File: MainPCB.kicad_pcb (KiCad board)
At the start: 4 copper layers, 108 x 70 mm, 70 parts, among them IC1 VNH7070ASTR, IC2 VNH7070ASTR, IC3 VNH7070ASTR, IC4 VNH7070ASTR, J1 Conn_01x06, J10 Conn_01x02, J11 Conn_01x03, J12 Conn_01x04, J2 RaspberryPi, J3 Conn_01x02, J4 Conn_01x02, J5 Screw_Terminal_01x02, J6 Conn_02x05_Odd_Even, J7 Conn_01x03, J8 Conn_01x02, J9 Conn_01x02, M1 Motor_DC, M2 Motor_DC, M3 Motor_DC, M4 Motor_DC, SW1 SW_DPST_x2, SW2 SW_SPDT, SW3 SW_SPDT, SW4 SW_SPDT, SW5 SW_SPDT, U1 V_Regulator3.3v, U10 N channel, U12 Teensy4.1, U2 V_Regulator5v, U4 V_Regulator5v, U5 Compass

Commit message: Finished Main PCB
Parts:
- R12, R13, R14, R15, R16, R17: moved to F.Cu
- moved R14 5.65 mm to (93.0, 88.2), turned to -90 degrees
- moved J4 3.43 mm to (123.2, 124.1), turned to 90 degrees
- moved R13 2.63 mm to (91.0, 84.4), turned to -90 degrees
- moved J8 1.19 mm to (88.4, 66.6)
- moved U1 1.04 mm to (85.8, 79.5)
- moved C7 0.60 mm to (97.6, 72.3)
- moved R12 0.57 mm to (93.0, 84.4), turned to -90 degrees
- moved C8 0.34 mm to (97.6, 69.8)
- turned R15 to 0 degrees
- turned R16 to 0 degrees
- turned R17 to 0 degrees
- turned R11 to 0 degrees
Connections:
- IC1 pad 12: 12v -> 12V
- IC1 pad 4: 12v -> 12V
- IC1 pad 5: 12v -> 12V
- IC2 pad 12: 12v -> 12V
- IC2 pad 4: 12v -> 12V
- IC2 pad 5: 12v -> 12V
- IC3 pad 12: 12v -> 12V
- IC3 pad 4: 12v -> 12V
- IC3 pad 5: 12v -> 12V
- IC4 pad 12: 12v -> 12V
- IC4 pad 4: 12v -> 12V
- IC4 pad 5: 12v -> 12V
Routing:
- net GND: track 8.32 -> 492.6 mm, vias 0 -> 2
- net 5V: track 0.00 -> 278.0 mm
- net 3.3V: track 0.00 -> 268.0 mm, vias 0 -> 1
- net 12V: track 140.3 -> 388.4 mm, vias 0 -> 36
- net Net-(SW1A-B): track 4.74 -> 120.5 mm, vias 0 -> 1
- net SLIDE3: track 0.00 -> 82.9 mm
- net SLIDE1: track 0.00 -> 78.2 mm
- net TX2->RX: track 0.00 -> 77.9 mm
- net RX2->TX: track 0.00 -> 76.6 mm, vias 0 -> 1
- net ESC_PWM: track 0.00 -> 75.2 mm
- net SLIDE2: track 0.00 -> 67.9 mm
- net CS3: track 0.00 -> 67.6 mm, vias 0 -> 1
- net CS2: track 0.00 -> 63.9 mm
- net STATE: track 0.00 -> 61.7 mm, vias 0 -> 1
- net CS1: track 0.00 -> 61.3 mm, vias 0 -> 1
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- added copper zone on B.Cu, net GND
- added copper zone on F.Cu, net GND
- added copper zone on In1.Cu, net GND
- added copper zone on In2.Cu, net GND

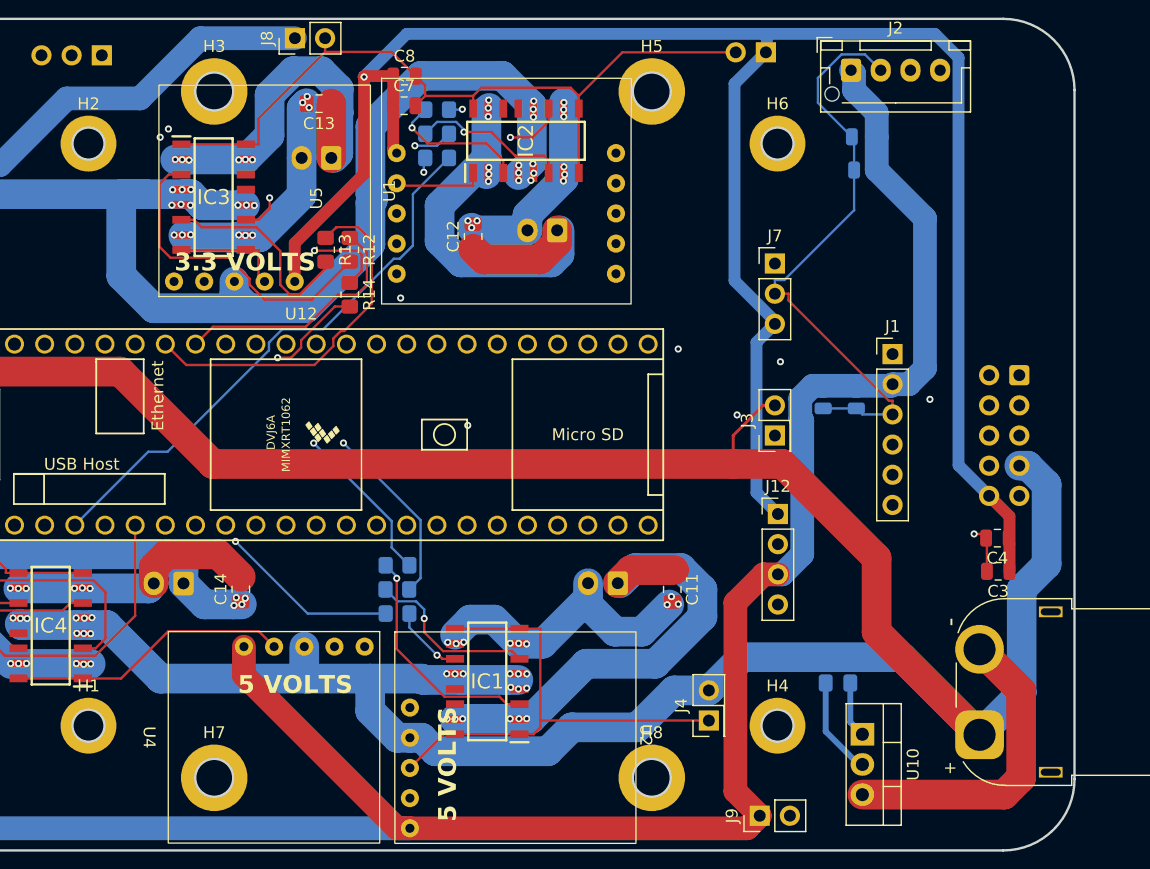
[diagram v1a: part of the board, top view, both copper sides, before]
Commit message: Fixed Holes error
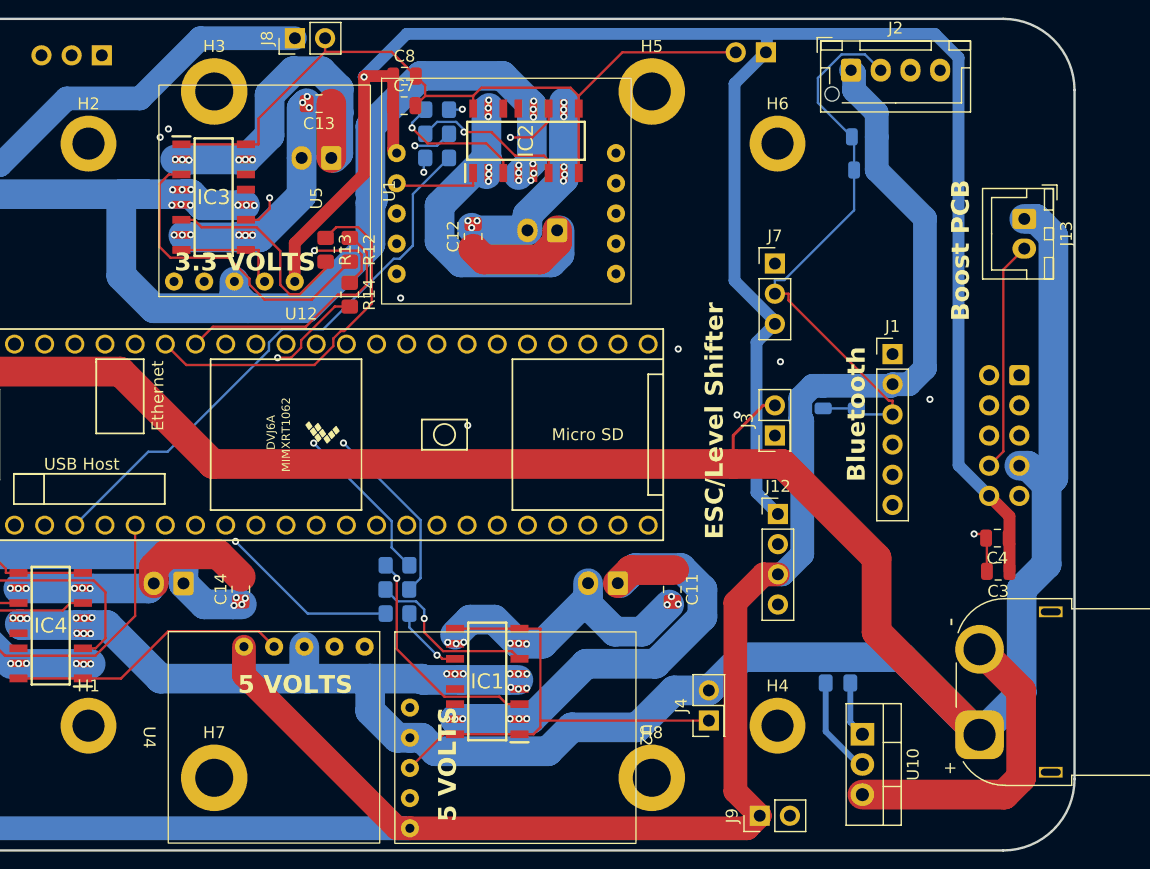
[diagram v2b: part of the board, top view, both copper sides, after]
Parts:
- added J13: Conn_01x02, Connector_JST:JST_XH_B2B-XH-A_1x02_P2.50mm_Vertical, F.Cu at (149.8, 81.8)
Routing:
- net 12V: track 388.4 -> 412.6 mm
- net GND: track 492.6 -> 512.1 mm
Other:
- outline, holes or cut-outs redrawn
- board text added: "Bluetooth"
- board text added: "Boost PCB"
- board text added: "ESC/Level Shifter"

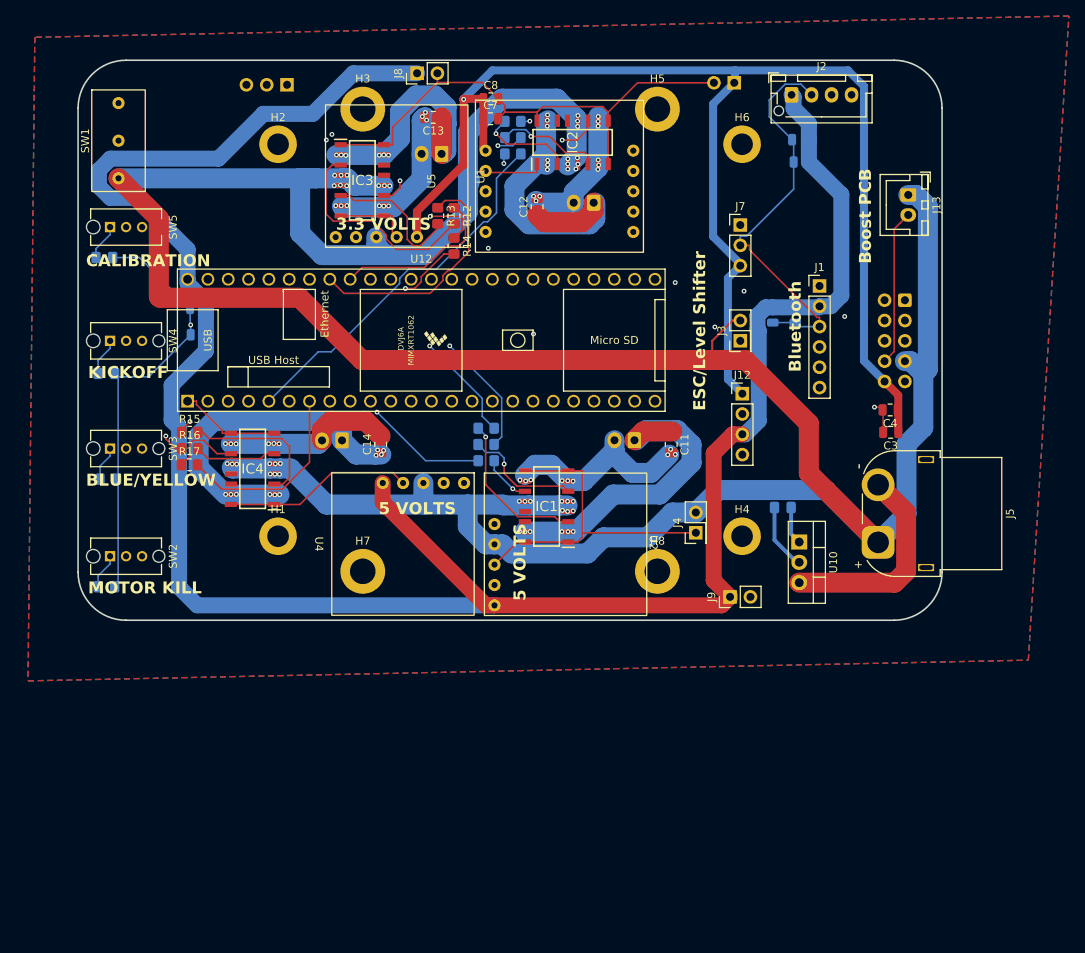
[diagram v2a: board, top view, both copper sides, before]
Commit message: Added Boost Converter
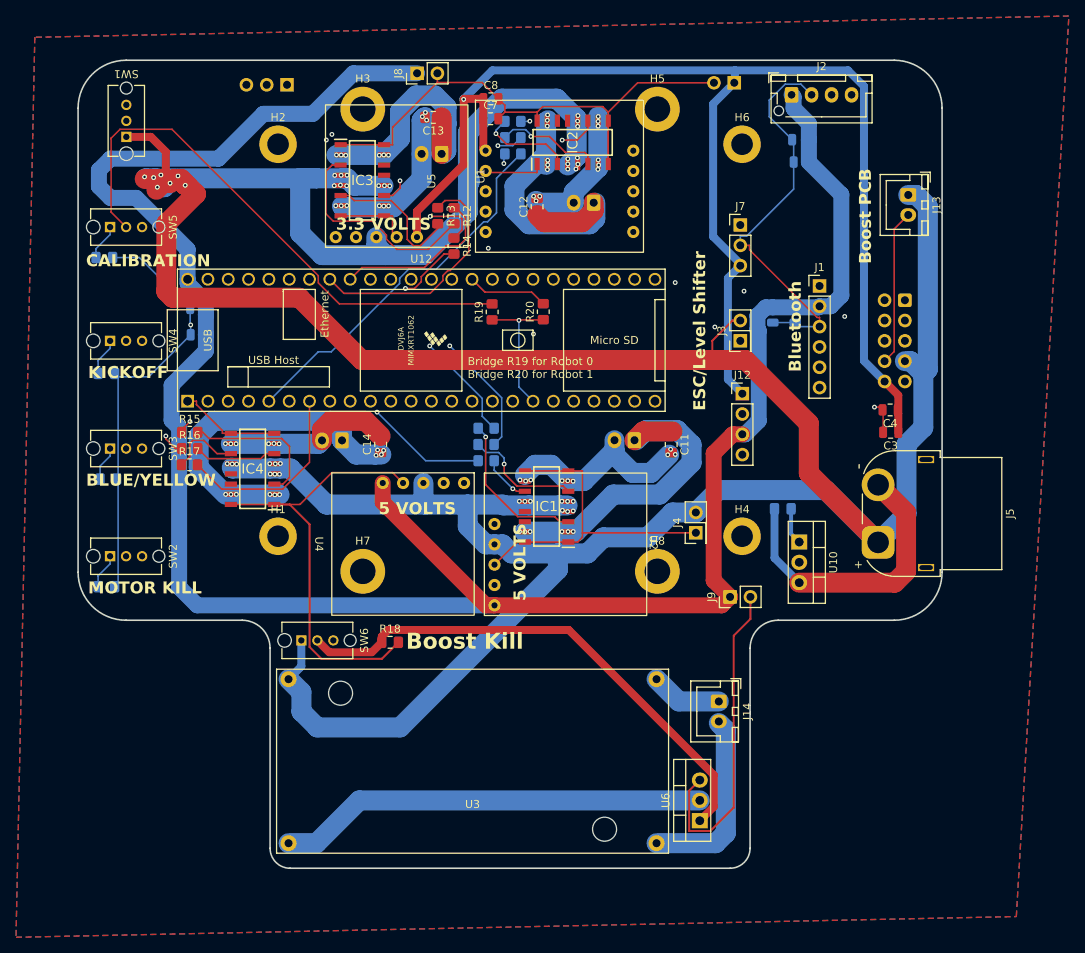
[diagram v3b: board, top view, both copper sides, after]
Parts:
- added J14: Conn_01x02, Connector_JST:JST_XH_B2B-XH-A_1x02_P2.50mm_Vertical, F.Cu at (126.1, 145.2)
- added R18: 10k, Capacitor_SMD:C_0805_2012Metric_Pad1.18x1.45mm_HandSolder, F.Cu at (85.0, 137.8)
- added R19: 0, Resistor_SMD:R_0805_2012Metric_Pad1.20x1.40mm_HandSolder, F.Cu at (97.8, 96.5)
- added R20: 1, Resistor_SMD:R_0805_2012Metric_Pad1.20x1.40mm_HandSolder, F.Cu at (104.2, 96.4)
- added SW6: SW_DPST_x2, SlideSW:SPDT_OS102011_CNK, F.Cu at (73.9, 137.5)
- added U3: BoostConverter, BoostConverter:Boost_Convertor_LM2577, F.Cu at (95.3, 152.6)
- added U6: N channel, Package_TO_SOT_THT:TO-220-3_Vertical, F.Cu at (123.7, 160.1)
- SW1: footprint ToggleSwitch:ANT11SECQE -> SlideSW:SPDT_OS102011_CNK
- moved SW1 1.09 mm to (52.0, 74.6), turned to 180 degrees
- moved R2 0.17 mm to (134.1, 121.1)
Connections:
- R2 pad 2: GND -> Net-(J5-Pin_2)
- U12 pad 18: unconnected-(U12-26_A12_MOSI1-Pad18) -> SelectionPin
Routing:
- net GND: track 512.1 -> 588.4 mm
- net 3.3V: track 268.0 -> 344.2 mm
- net 12V: track 412.6 -> 478.6 mm, vias 36 -> 43
- net Net-(SW6A-B): track 0.00 -> 65.7 mm
- net Net-(U3-In-): track 0.00 -> 53.6 mm
- net Net-(J14-Pin_2): track 0.00 -> 23.3 mm
- net SelectionPin: track 0.00 -> 17.3 mm, vias 0 -> 1
- net Net-(J5-Pin_2): track 26.2 -> 36.7 mm
- net Net-(J14-Pin_1): track 0.00 -> 8.93 mm
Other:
- board size 108 x 70 mm -> 108 x 101 mm
- board text added: "Boost Kill"
- board text added: "Bridge R19 for Robot 0 Bridge R20 for Robot 1"

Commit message: Flipped JST Motor Connectors
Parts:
- M1, M2, M3, M4: moved to F.Cu
- moved M1 1.74 mm to (115.8, 114.2)
- moved M4 0.75 mm to (79.0, 113.3)
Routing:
- net 12V: track 478.6 -> 472.2 mm
- net Net-(IC1-OUT_A_1): track 46.6 -> 49.1 mm
- net Net-(IC1-OUT_B_1): track 28.4 -> 30.0 mm
- net Net-(IC4-OUT_B_1): track 22.2 -> 23.0 mm

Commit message: changed a lot
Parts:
- removed J12: Conn_01x04, Connector_PinHeader_2.54mm:PinHeader_1x04_P2.54mm_Vertical
- removed J3: Conn_01x02, Connector_PinHeader_2.54mm:PinHeader_2x01_P2.54mm_Vertical
- removed J7: Conn_01x03, Connector_PinHeader_2.54mm:PinHeader_1x03_P2.54mm_Vertical
- removed U5: Compass, Custom:Compass Sensor DFRobot
- added C15: 0.1uf, Capacitor_SMD:C_0805_2012Metric_Pad1.18x1.45mm_HandSolder, B.Cu at (139.7, 80.3)
- added IC5: VNH7070ASTR, VNH:SOIC127P600X175-16N, F.Cu at (130.8, 83.8)
- added J15: Conn_01x05, Connector_JST:JST_XH_B5B-XH-A_1x05_P2.50mm_Vertical, F.Cu at (59.8, 77.6)
- added J16: Conn_01x05, Connector_JST:JST_XH_B5B-XH-A_1x05_P2.50mm_Vertical, F.Cu at (150.0, 75.6)
- added M5: Motor_DC, Connector_JST:JST_XH_B2B-XH-AM_1x02_P2.50mm_Vertical, F.Cu at (139.2, 86.5)
- added R21: 10k, Capacitor_SMD:C_0805_2012Metric, F.Cu at (64.4, 85.0)
- added R22: 15k, Capacitor_SMD:C_0805_2012Metric, F.Cu at (64.4, 88.1)
- added R23: 100, Resistor_SMD:R_0805_2012Metric_Pad1.20x1.40mm_HandSolder, B.Cu at (119.1, 85.3)
- added R24: 100, Resistor_SMD:R_0805_2012Metric_Pad1.20x1.40mm_HandSolder, B.Cu at (128.8, 90.9)
- added R25: 100, Resistor_SMD:R_0805_2012Metric_Pad1.20x1.40mm_HandSolder, B.Cu at (136.7, 91.2)
- added U7: 4554, 4554:MODULE_4554, F.Cu at (116.6, 77.5)
- J13: value Conn_01x02 -> Conn_01x03; footprint Connector_JST:JST_XH_B2B-XH-A_1x02_P2.50mm_Vertical -> Connector_PinHeader_2.54mm:PinHeader_1x03_P2.54mm_Vertical
- moved J13 108.3 mm to (49.0, 121.7), turned to 90 degrees
- moved C12 10.2 mm to (113.3, 81.1)
- moved M2 5.04 mm to (106.5, 86.0)
- moved C13 0.62 mm to (90.5, 71.5)
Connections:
- J13 pad 1: 12V -> 3.3V
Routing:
- net Net-(J15-Pin_5): track 0.00 -> 229.2 mm, vias 0 -> 1
- net TRIG4: track 0.00 -> 92.6 mm
- net ESC_PWM: track 75.2 -> 0.00 mm
- net PWM5: track 0.00 -> 67.8 mm, vias 0 -> 1
- net TRIG3: track 0.00 -> 67.5 mm, vias 0 -> 1
- net ECHO: track 0.00 -> 59.9 mm
- net TRIG2: track 0.00 -> 54.9 mm
- net TRIG1: track 0.00 -> 47.3 mm
- net GND: track 588.4 -> 621.5 mm, vias 2 -> 3
- net SDA2: track 25.1 -> 54.4 mm
- net SCL2: track 27.5 -> 54.0 mm
- net Net-(IC5-OUT_B_1): track 0.00 -> 25.8 mm, vias 0 -> 4
- net Net-(IC5-PWM): track 0.00 -> 21.9 mm, vias 0 -> 1
- net 5V: track 278.0 -> 297.8 mm, vias 0 -> 1
- net Net-(IC5-OUT_A_1): track 0.00 -> 19.1 mm, vias 0 -> 4
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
